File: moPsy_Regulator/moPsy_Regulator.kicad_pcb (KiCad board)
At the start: 2 copper layers, 96.5 x 44.5 mm, 28 parts, among them J1 Conn_01x01_Pin, J2 Conn_01x01_Pin, J3 Conn_01x01_Pin, J4 Conn_01x01_Pin, Q1 BD201, Q2 BC337, U1 LM723_DIP14

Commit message: Improve the circuit
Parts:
- removed JP1, JP2, JP3, JP4, JP5, JP6: SolderJumper_2_Open, Jumper:SolderJumper-2_P1.3mm_Open_RoundedPad1.0x1.5mm
- removed R1, R3: "R1"/"R3", Resistor_THT:R_Axial_DIN0207_L6.3mm_D2.5mm_P7.62mm_Horizontal
- added D2: 1N4001, Diode_THT:D_DO-41_SOD81_P7.62mm_Horizontal, F.Cu at (133.3, 80.0)
- added R7: 2k7 1%, Resistor_THT:R_Axial_DIN0207_L6.3mm_D2.5mm_P7.62mm_Horizontal, F.Cu at (126.4, 88.3)
- added R8: 2k7 1%, Resistor_THT:R_Axial_DIN0207_L6.3mm_D2.5mm_P7.62mm_Horizontal, F.Cu at (122.6, 80.6)
- R2: value "R2" -> 1k
- RV1: value "P1" -> 5k
- moved REF1 88.9 mm to (194.3, 69.8)
- moved REF2 88.9 mm to (105.4, 69.8)
- moved C5 57.1 mm to (137.6, 87.6)
- moved RV1 18.6 mm to (107.8, 81.4), turned to -90 degrees
- moved C4 13.4 mm to (194.3, 80.0), turned to 180 degrees
- moved R4 4.45 mm to (141.0, 76.8)
- moved R2 3.99 mm to (118.7, 80.6), turned to -90 degrees
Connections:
- net LV_{center} renamed Net-(U1-+)
- C1 pad 2: HV_{center} -> Net-(U1--)
- C5 pad 1: V_{out} -> Net-(D2-K)
- RV1 pad 1: Net-(JP11-B) -> V_{out}
- RV1 pad 2: Net-(JP12-B) -> Net-(U1--)
- U1 pad 11: V_{in} -> Net-(D2-K)
- U1 pad 12: V_{in} -> Net-(D2-K)
- U1 pad 4: HV_{center} -> Net-(U1--)
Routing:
- net HV_{center}: track 40.7 -> 0.00 mm
- net Net-(JP12-B): track 37.9 -> 0.00 mm, vias 1 -> 0
- net Net-(U1--): track 0.00 -> 31.5 mm
- net Net-(D2-K): track 0.00 -> 29.6 mm
- net HV_{top}: track 28.5 -> 0.00 mm
- net Net-(JP11-B): track 25.4 -> 0.00 mm, vias 1 -> 0
- net V_{in}: track 142.3 -> 118.5 mm
- net Net-(U1-+): track 41.0 -> 21.9 mm, vias 2 -> 0
- net LV_{top}: track 13.3 -> 0.00 mm
- net V_{out}: track 194.9 -> 182.8 mm
- net Net-(Q2-B): track 34.4 -> 30.5 mm
- net Net-(Q1-B): track 12.1 -> 14.2 mm
- net Net-(U1-VREF): track 14.3 -> 12.2 mm
- net Net-(R2-Pad1): track 4.92 -> 6.20 mm
- net Net-(D1-A): track 74.9 -> 74.8 mm, vias 1 -> 0
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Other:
- board text removed: "12V"
- board text removed: "1k5"
- board text removed: "2k7"
- board text removed: "470"
- board text removed: "5V"
- board text removed: "<7V"
- board text removed: ">7V"
- board text removed: "Bridge one group:"
- board text removed: "Order"
- board text removed: "R1"
- board text removed: "R1/R3"
- board text removed: "R2"
- board text removed: "R3"
- board text removed: "R3/R1"

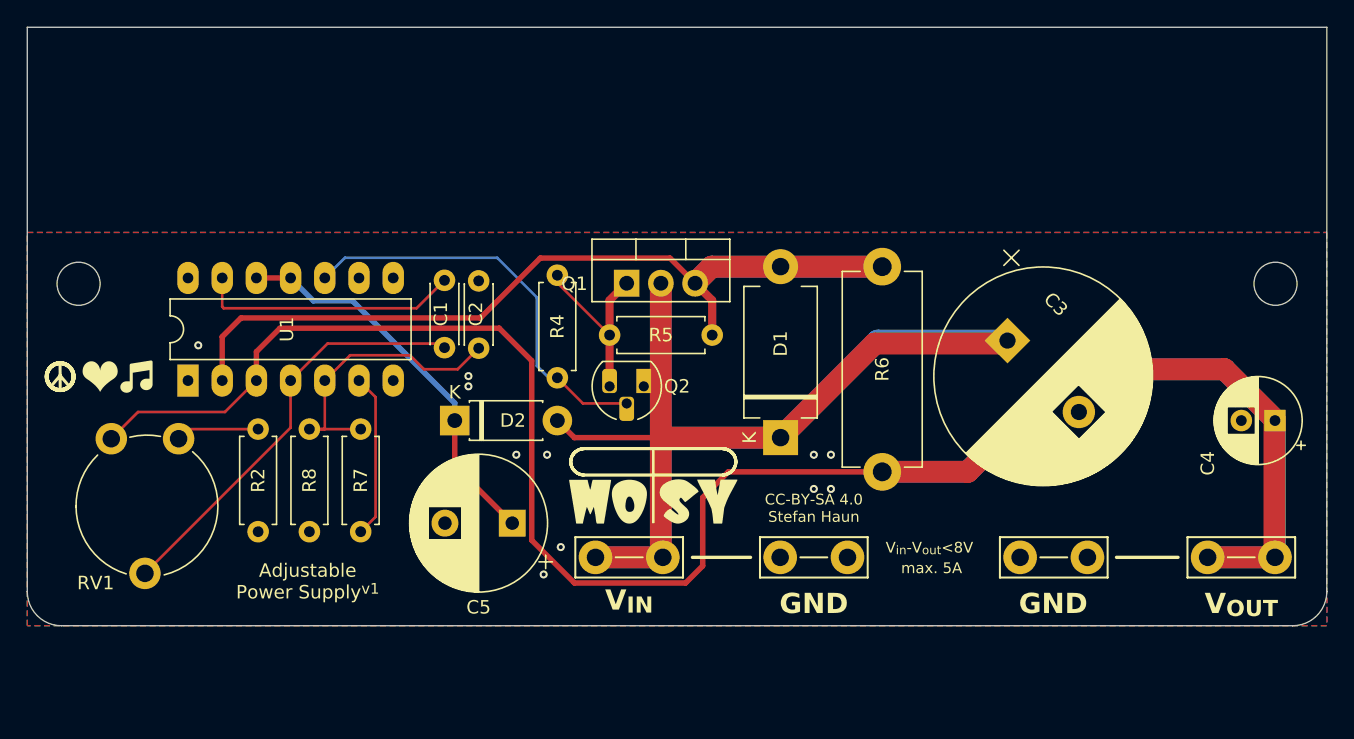
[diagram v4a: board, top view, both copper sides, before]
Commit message: Set hole positions and board outline
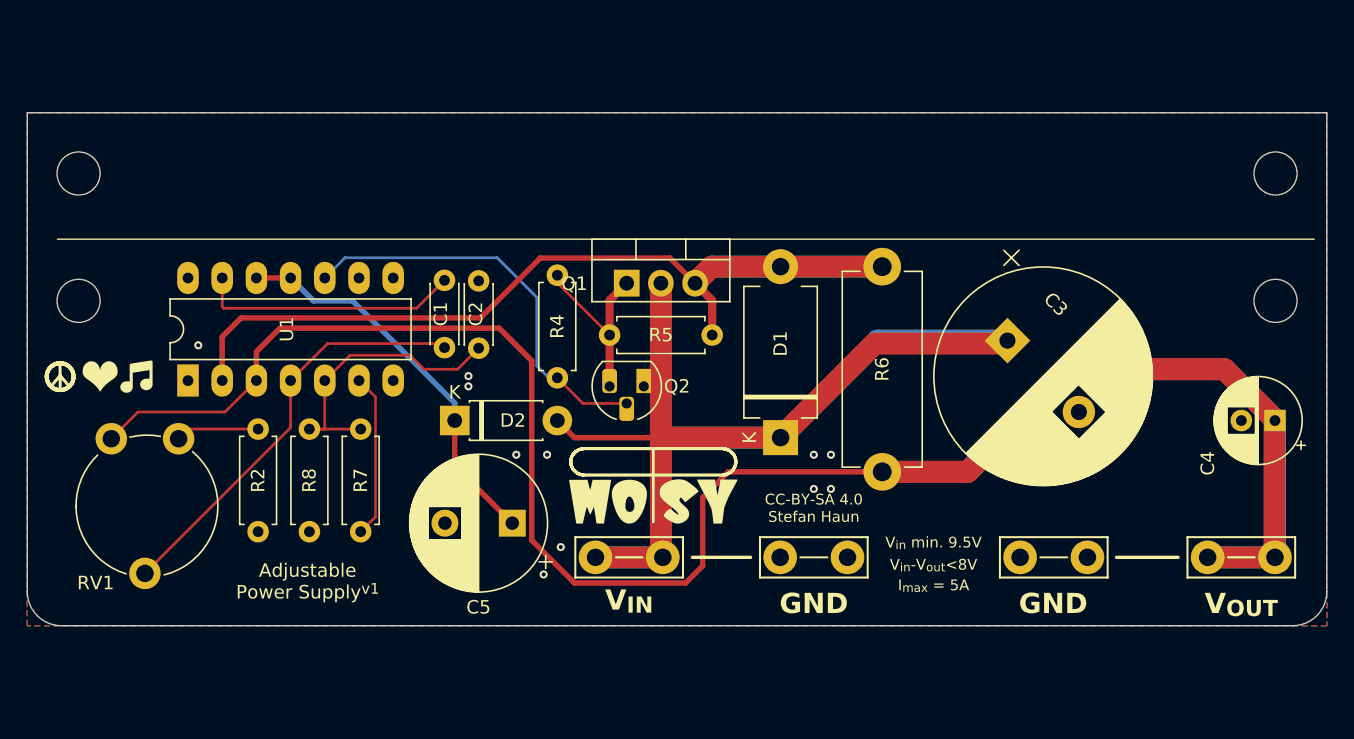
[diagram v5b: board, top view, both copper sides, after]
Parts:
- added REF1: MountingHole_3.2mm_M3, MountingHole:MountingHole_3.2mm_M3, F.Cu at (194.3, 61.7)
- added REF2: MountingHole_3.2mm_M3, MountingHole:MountingHole_3.2mm_M3, F.Cu at (105.4, 61.7)
- moved REF1 1.27 mm to (194.3, 71.1)
- moved REF2 1.27 mm to (105.4, 71.1)
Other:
- board size 96.5 x 44.5 mm -> 96.5 x 38.1 mm
- board text added: "I_{max} = 5A"
- board text added: "V_{in} min. 9.5V"
- board text removed: "max. 5A"
